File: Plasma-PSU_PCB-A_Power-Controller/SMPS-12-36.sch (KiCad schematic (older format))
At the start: 58 parts, among them J501 Probe_Vin, J502 Probe_Iin, J503 JP_RUN, J504 Probe_Iout, J505 Probe_Vout, J506 Probe_DAC_A, J507 Probe_DAC_B, J508 OPAMP_Vout, J509 OPAMP_Iout, Q501 NVTFS6H850NL, Q502 NVTFS6H850NL, U501 MCP602, U502 MCP602, U503 LTC3786, U504 MCP4822

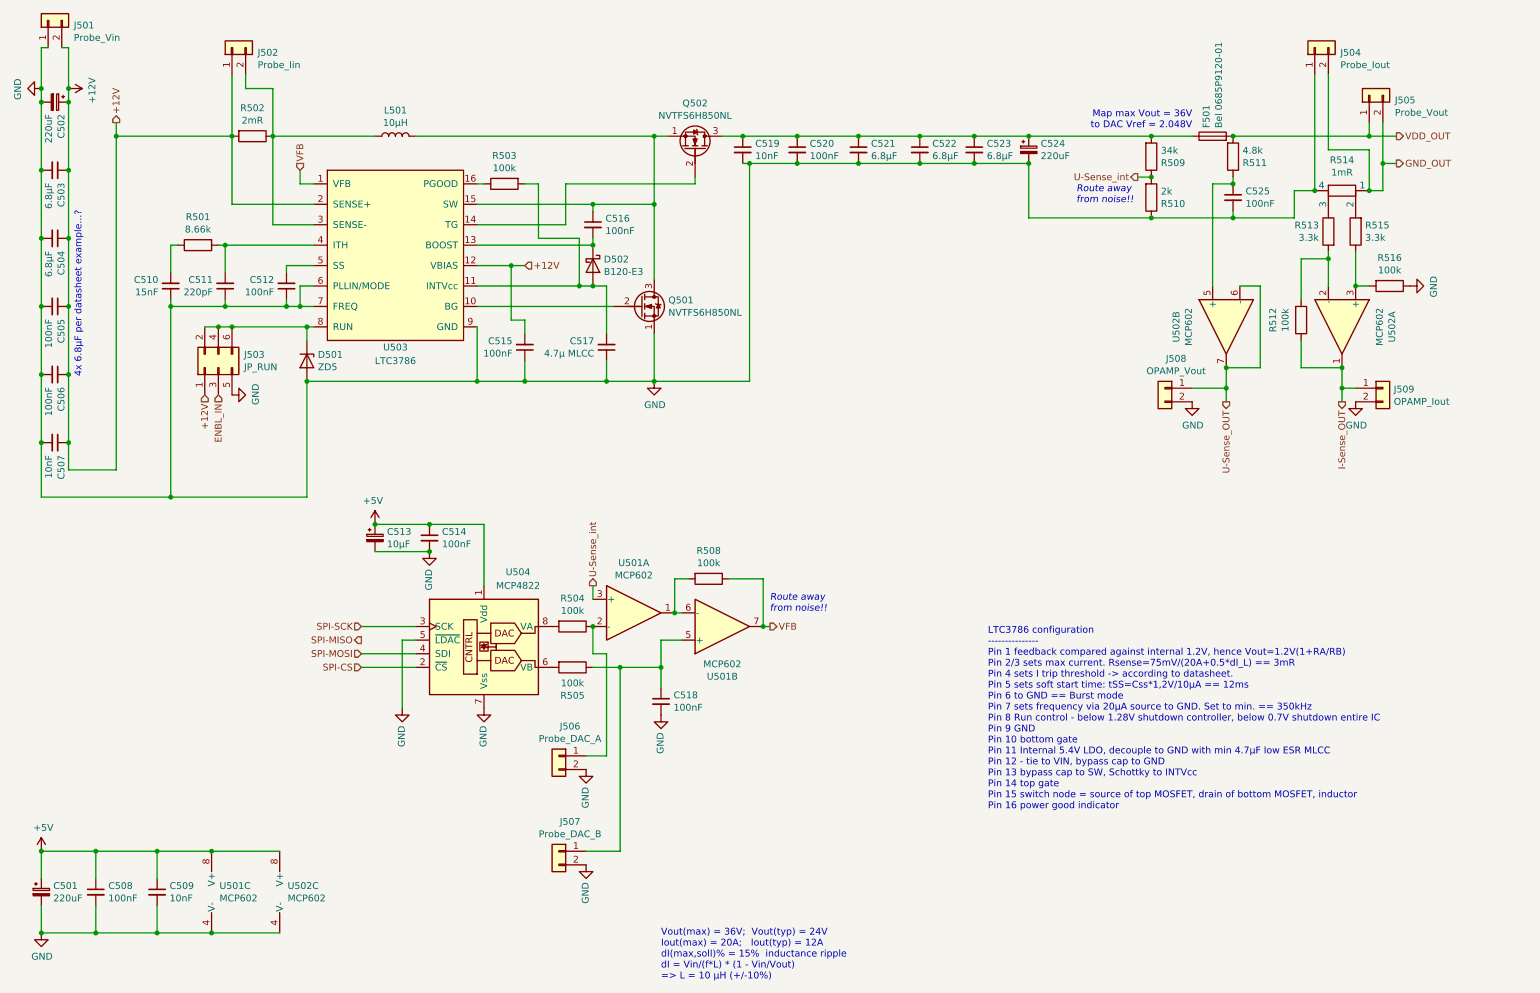
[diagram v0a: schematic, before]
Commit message: BOM PCB-B arranged
Order numbers for Farnell-element14 and for Mouser
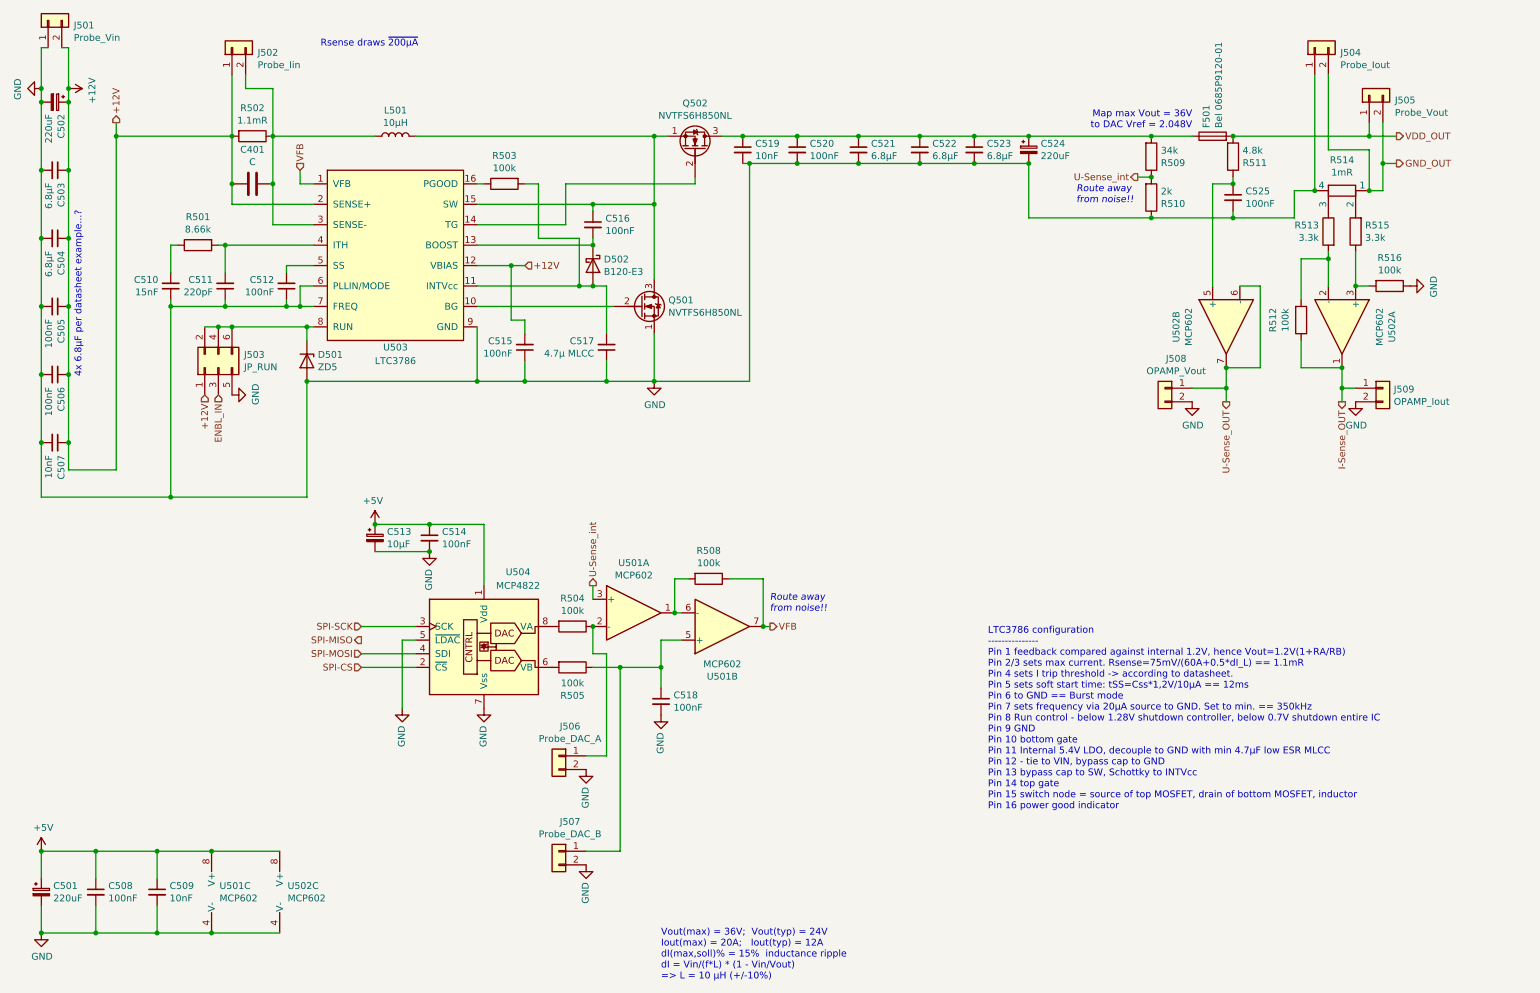
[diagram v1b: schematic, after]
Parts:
- added C401: C, symbol Device:C
- R502: value 2mR -> 1.1mR
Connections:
- net +12V: now also C401.1
- net at J502.2 (Pin_2), L501.1, R502.1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: now also C401.2
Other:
- note added: "LTC3786 configuration\n---------------\nPin 1 feedback compared against internal 1.2V, hence Vout=1.2V(1+RA/RB)\nPin 2/3 sets max current. Rsense=75mV/(60A+0.5*dI_L) == 1.1mR \nPin 4 sets I trip threshold -> according to datasheet.\nPin 5 sets soft start time: tSS=Css*1,2V/10µA == 12ms\nPin 6 to GND == Burst mode\nPin 7 sets frequency via 20µA source to GND. Set to min. == 350kHz\nPin 8 Run contr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"
- note added: "Rsense draws ~200µA"
- note removed: "LTC3786 configuration\n---------------\nPin 1 feedback compared against internal 1.2V, hence Vout=1.2V(1+RA/RB)\nPin 2/3 sets max current. Rsense=75mV/(20A+0.5*dI_L) == 3mR \nPin 4 sets I trip threshold -> according to datasheet.\nPin 5 sets soft start time: tSS=Css*1,2V/10µA == 12ms\nPin 6 to GND == Burst mode\nPin 7 sets frequency via 20µA source to GND. Set to min. == 350kHz\nPin 8 Run control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"
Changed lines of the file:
@@
 P 2350 1450
 F 0 "R502" V 2143 1450 50  0000 C CNN
-F 1 "2mR" V 2234 1450 50  0000 C CNN
+F 1 "1.1mR" V 2234 1450 50  0000 C CNN
 F 2 "Resistor_SMD:R_2512_6332Metric" V 2280 1450 50  0001 C CNN
 F 3 "~" H 2350 1450 50  0001 C CNN
@@
 $EndComp
 Wire Wire Line
-	2200 1450 2200 1950
+	2200 1450 2200 1800
 Wire Wire Line
 	2200 1950 2800 1950
 Wire Wire Line
-	2500 1450 2500 2100
+	2500 1450 2500 1800
 Wire Wire Line
 	2500 2100 2800 2100
@@
 	4850 2550 4950 2550
 Text Notes 7750 6400 0    50   ~ 0
-LTC3786 configuration\n---------------\nPin 1 feedback compared against internal 1.2V, hence Vout=1.2V(1+RA/RB)\nPin 2/3 sets max current. Rsense=75mV/(20A+0.5*dI_L) == 3mR \nPin 4 sets I trip threshold -> according to datasheet.\nPin 5 sets soft start time: tSS=Css*1,2V/10µA == 12ms\nPin 6 to GND == Burst mode\nPin 7 sets frequency via 20µA source to GND. Set to min. == 350kHz\nPin 8 Run control - below 1.28V shutdown controller, below 0.7V shutdown entire IC\nPin 9 GND\nPin 10 bottom gate\nPin 11 Internal 5.4V LDO, decouple to GND with min 4.7µF low ESR MLCC\nPin 12 - tie to VIN, bypass cap to GND\nPin 13 bypass cap to SW, Schottky to INTVcc\nPin 14 top gate\nPin 15 switch node = source of top MOSFET, drain of bottom MOSFET, inductor\nPin 16 power good indicator
+LTC3786 configuration\n---------------\nPin 1 feedback compared against internal 1.2V, hence Vout=1.2V(1+RA/RB)\nPin 2/3 sets max current. Rsense=75mV/(60A+0.5*dI_L) == 1.1mR \nPin 4 sets I trip threshold -> according to datasheet.\nPin 5 sets soft start time: tSS=Css*1,2V/10µA == 12ms\nPin 6 to GND == Burst mode\nPin 7 sets frequency via 20µA source to GND. Set to min. == 350kHz\nPin 8 Run control - below 1.28V shutdown controller, below 0.7V shutdown entire IC\nPin 9 GND\nPin 10 bottom gate\nPin 11 Internal 5.4V LDO, decouple to GND with min 4.7µF low ESR MLCC\nPin 12 - tie to VIN, bypass cap to GND\nPin 13 bypass cap to SW, Schottky to INTVcc\nPin 14 top gate\nPin 15 switch node = source of top MOSFET, drain of bottom MOSFET, inductor\nPin 16 power good indicator
 Connection ~ 4850 1950
 Connection ~ 4850 2250
@@
 Wire Wire Line
 	2200 2850 2750 2850
+$Comp
+L Device:C C401
+U 1 1 5E983B74
+P 2350 1800
+F 0 "C401" V 2602 1800 50  0000 C CNN
+F 1 "C" V 2511 1800 50  0000 C CNN
+F 2 "" H 2388 1650 50  0001 C CNN
+F 3 "~" H 2350 1800 50  0001 C CNN
+	1    2350 1800
+	0    -1   -1   0
+$EndComp
+Connection ~ 2200 1800
+Wire Wire Line
+	2200 1800 2200 1950
+Connection ~ 2500 1800
+Wire Wire Line
+	2500 1800 2500 2100
+Text Notes 2850 800  0    50   ~ 0
+Rsense draws ~200µA
 $EndSCHEMATC

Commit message: Power Inductor updated
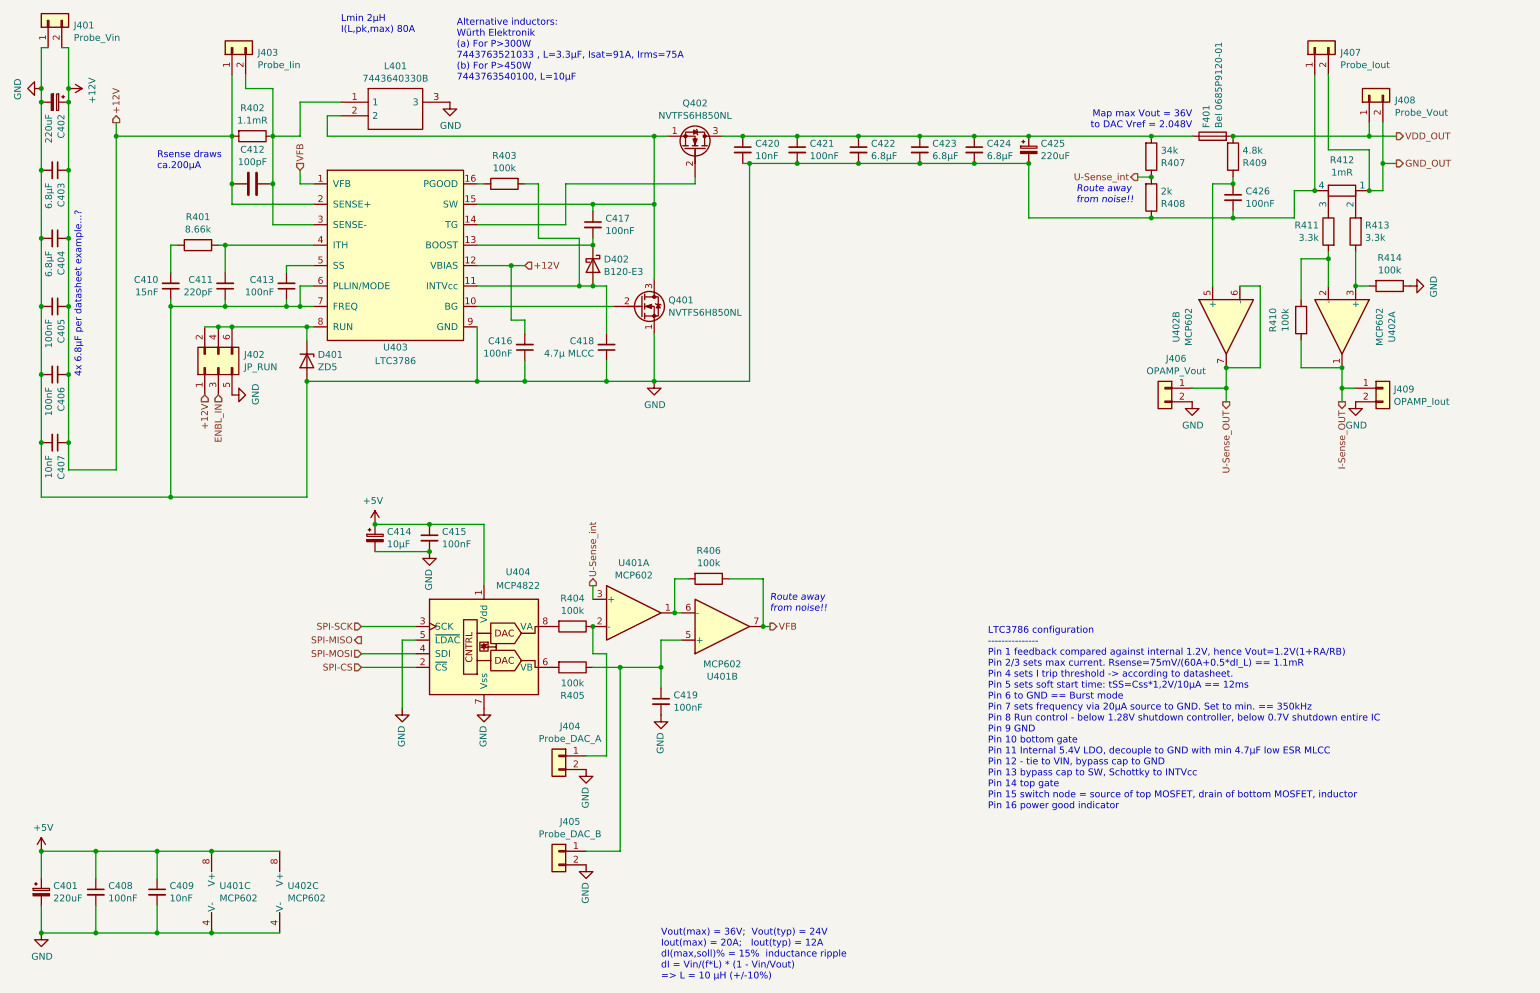
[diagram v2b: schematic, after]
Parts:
- removed L501: 10µH, symbol Device:L
- added L401: 7443640330B, SamacSys_PCB_library:7443640330B, symbol SamacSys_lib_loader:7443640330B
- C412: renamed from C401; value C -> 100pF; footprint (none) -> Capacitor_SMD:C_0402_1005Metric
- renumbered C501 to C401, C502 to C402, C503 to C403, C504 to C404, C505 to C405, C506 to C406, C507 to C407, C508 to C408, C509 to C409, C510 to C410, C511 to C411, C512 to C413, C513 to C414, C514 to C415, C515 to C416, C516 to C417, C517 to C418, C518 to C419, C519 to C420, C520 to C421, C521 to C422, C522 to C423, C523 to C424, C524 to C425, C525 to C426, D501 to D401, D502 to D402, F501 to F401, J501 to J401, J503 to J402, J502 to J403, J506 to J404, J507 to J405, J508 to J406, J504 to J407, J505 to J408, J509 to J409, Q501 to Q401, Q502 to Q402, R501 to R401, R502 to R402, R503 to R403, R504 to R404, R505 to R405, R508 to R406, R509 to R407, R510 to R408, R511 to R409, R512 to R410, R513 to R411, R514 to R412, R515 to R413, R516 to R414, U501 to U401, U502 to U402, U503 to U403, U504 to U404
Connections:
- net GND: now also L401.3
- net at C417.1, Q401.3 (D), Q402.1 (S)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: now also L401.2
- net at C412.2, J403.2 (Pin_2), R402.1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: now also L401.1
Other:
- note added: "Alternative inductors:\nWürth Elektronik\n(a) For P>300W\n7443763521033 , L=3.3µF, Isat=91A, Irms=75A\n(b) For P>450W\n7443763540100, L=10µF"
- note added: "Lmin 2µH\nI(L,pk,max) 80A"
- note added: "Rsense draws \nca.200µA"
- note removed: "Rsense draws ~200µA"

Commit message: FET & L revision w/ LTpowerCAD
LTpowerCAD tool used to revise selection of:
- main inductor
- control FET
- sync FET
- input and output capacitor banks
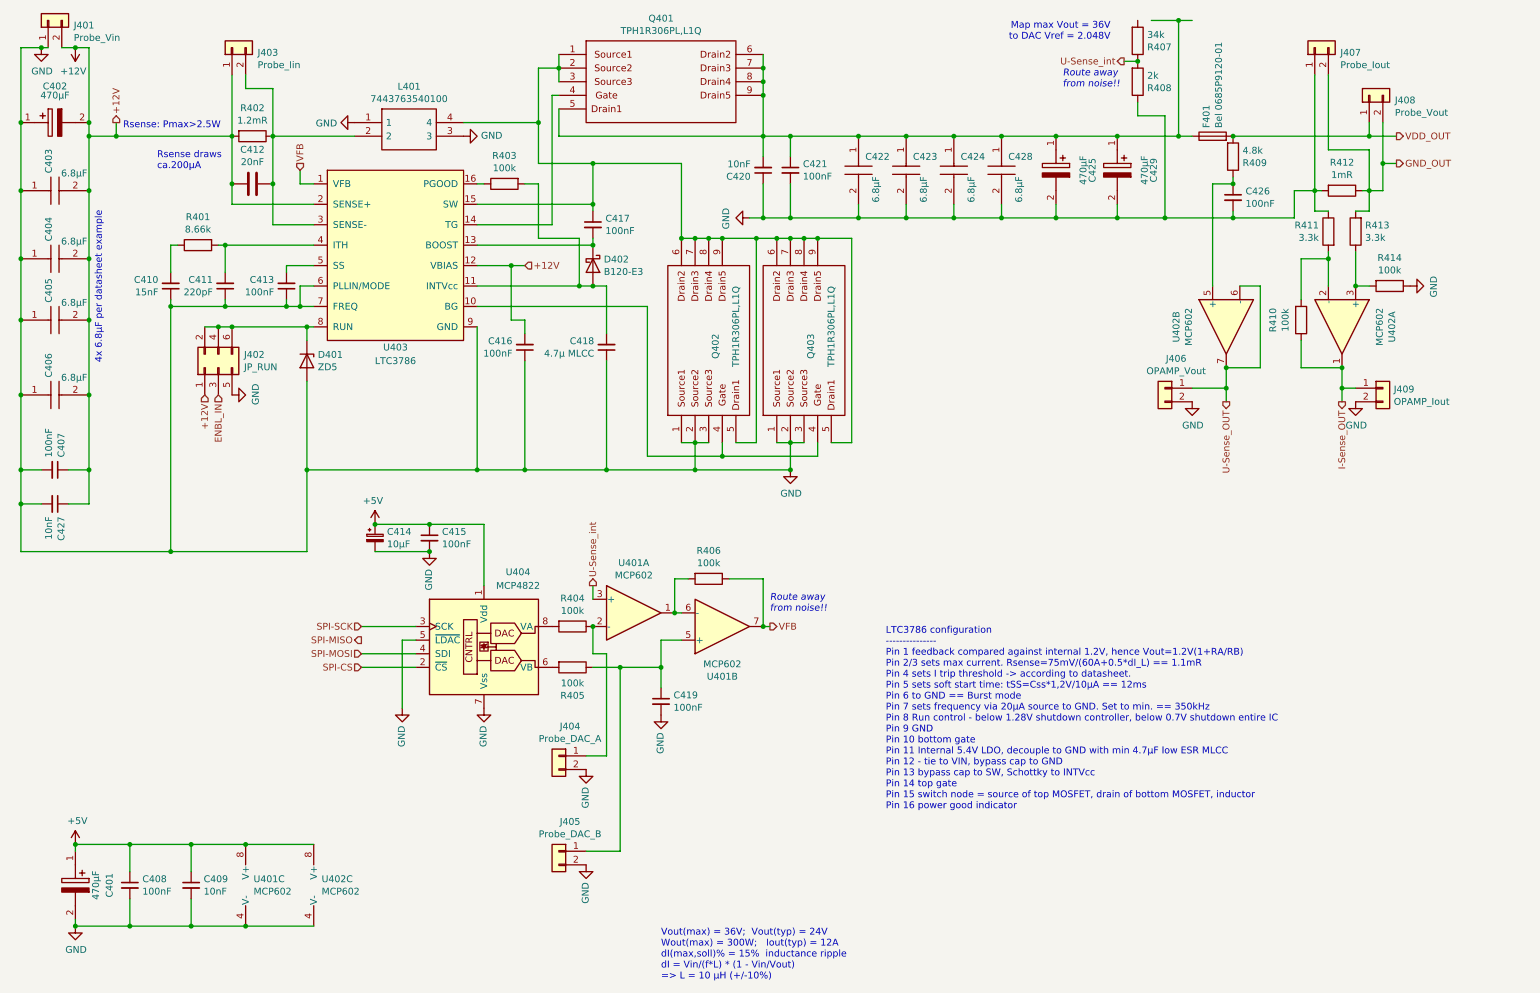
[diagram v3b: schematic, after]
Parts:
- removed C401, C402, C425: 220uF, Capacitor_THT:CP_Radial_D8.0mm_P3.50mm, symbol Device:CP_Small
- removed C403, C404, C422, C423, C424: 6.8µF, Capacitor_SMD:C_1206_3216Metric, symbol Device:C_Small
- removed C405, C406: 100nF, Capacitor_SMD:C_1206_3216Metric, symbol Device:C_Small
- removed L401: 7443640330B, SamacSys_PCB_library:7443640330B, symbol SamacSys_lib_loader:7443640330B
- removed Q401, Q402: NVTFS6H850NL, Plasma-PSU_PCB-A_Power-Controller:ONSEMI-µ8FL, symbol Device:Q_NMOS_SGD
- removed R412: 1mR, Resistor_SMD:R_2512_6332Metric, symbol Device:R_Shunt
- added C401, C402, C425, C429: EEHZS1V471P, CAPAE1030X1680N, symbol SamacSys_lib_loader:EEHZS1V471P
- added C403, C404, C405, C406, C422, C423, C424, C428: C4532X7R1H685M250KB, CAPC4532X360N, symbol SamacSys_lib_loader:C4532X7R1H685M250KB
- added C427: 10nF, Capacitor_SMD:C_0805_2012Metric, symbol Device:C_Small
- added L401: 7443763540100, SamacSys_PCB_library:7443763540100, symbol SamacSys_lib_loader:7443763540100
- added Q401, Q402, Q403: TPH1R306PL,L1Q, TPH1R306PLL1Q, symbol SamacSys_lib_loader:TPH1R306PL,L1Q
- added R412: 1mR, Resistor_SMD:R_2512_6332Metric, symbol Device:R
- C407: value 10nF -> 100nF
- C412: value 100pF -> 20nF
- R402: value 1.1mR -> 1.2mR
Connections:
- net +12V: now also C402.2, C403.2, C404.2, C405.2, C406.2, C427.1
- net +5V: now also C401.1
- net GND: now also C420.1, R411.1, C401.2, C402.1, C403.1, C404.1, C405.1, C406.1, C422.2, C423.2, C424.2, C425.2, C427.2, C428.2, C429.2, L401.1, L401.3, Q402.1, Q402.2, Q402.3, Q403.1, Q403.2, Q403.3, R412.2; no longer C420.2
- net GND_OUT: now also R413.2, R412.1
- net at C421.1, F401.1: now also C420.2, C422.1, C423.1, C424.1, C425.1, C428.1, C429.1, Q401.5, Q401.6, Q401.7, Q401.8, Q401.9; no longer C420.1, R407.2
- net at U403.10 (BG): now also Q402.4, Q403.4
- net at C417.1, U403.15 (SW): now also L401.4, Q401.1, Q401.2, Q401.3, Q402.5, Q402.6, Q402.7, Q402.8, Q402.9, Q403.5, Q403.6, Q403.7, Q403.8, Q403.9
- net at U403.14 (TG): now also Q401.4
- net at C412.2, J403.2 (Pin_2), R402.1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: now also L401.2
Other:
- note added: "4x 6.8µF per datasheet example"
- note added: "Rsense: Pmax>2.5W"
- note added: "Vout(max) = 36V; Vout(typ) = 24V\nWout(max) = 300W; Iout(typ) = 12A\ndI(max,soll)% = 15% inductance ripple\ndI = Vin/(f*L) * (1 - Vin/Vout)\n=> L = 10 µH (+/-10%)"
- note removed: "4x 6.8µF per datasheet example...?"
- note removed: "Alternative inductors:\nWürth Elektronik\n(a) For P>300W\n7443763521033 , L=3.3µF, Isat=91A, Irms=75A\n(b) For P>450W\n7443763540100, L=10µF"
- note removed: "Lmin 2µH\nI(L,pk,max) 80A"
- note removed: "Vout(max) = 36V; Vout(typ) = 24V\nIout(max) = 20A; Iout(typ) = 12A\ndI(max,soll)% = 15% inductance ripple\ndI = Vin/(f*L) * (1 - Vin/Vout)\n=> L = 10 µH (+/-10%)"
- moved on the sheet: C407, C408, C409, C420, C421, R407, R408, U401C, U402C
